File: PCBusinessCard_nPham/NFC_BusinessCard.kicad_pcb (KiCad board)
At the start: 2 copper layers, 85.6 x 68.1 mm, 20 parts

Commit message: front side done
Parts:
- removed the ? at (80.0, 43.1)
- removed the ? at (79.0, 46.2)
- removed the ? at (73.2, 47.8)
- moved LED1 21.1 mm to (94.0, 55.9)
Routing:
- net N$4: track 55.8 -> 54.4 mm, vias 2 -> 1
- net N$6: track 70.7 -> 69.3 mm, vias 2 -> 1

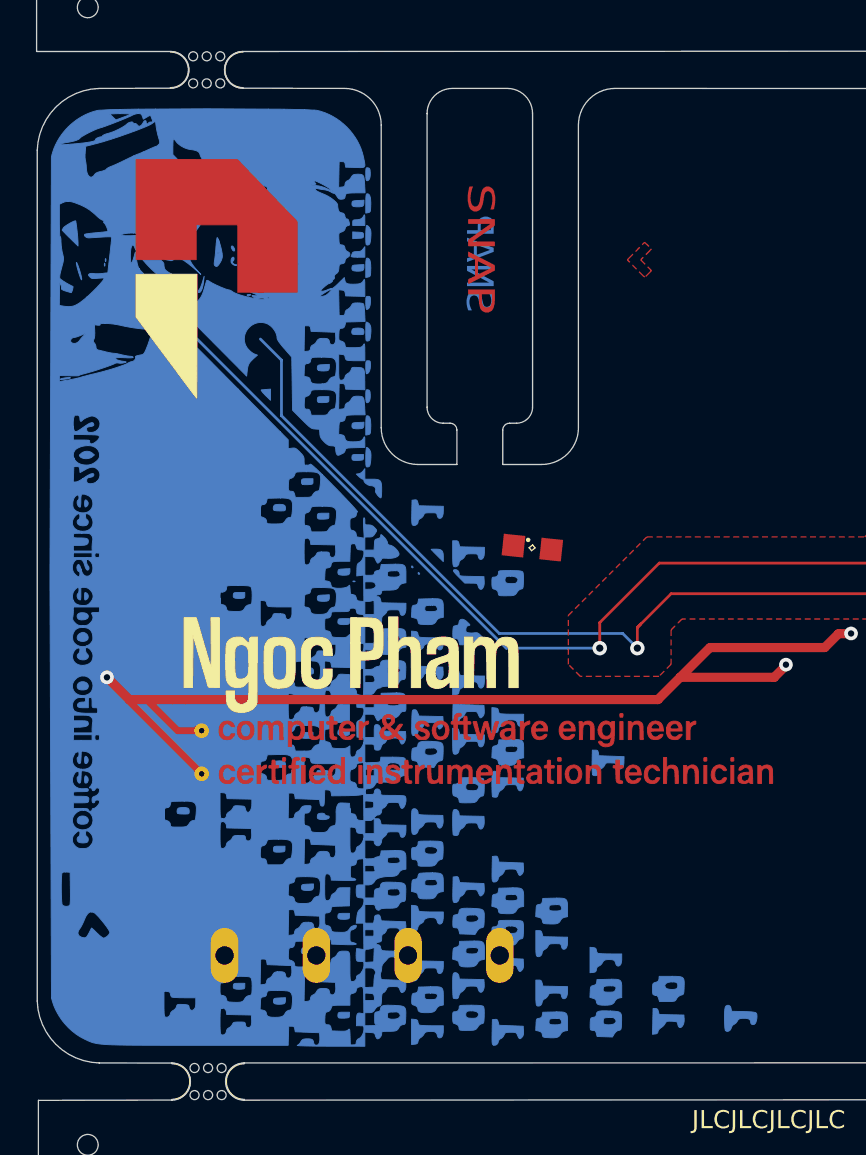
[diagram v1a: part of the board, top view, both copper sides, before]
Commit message: finished front and back side
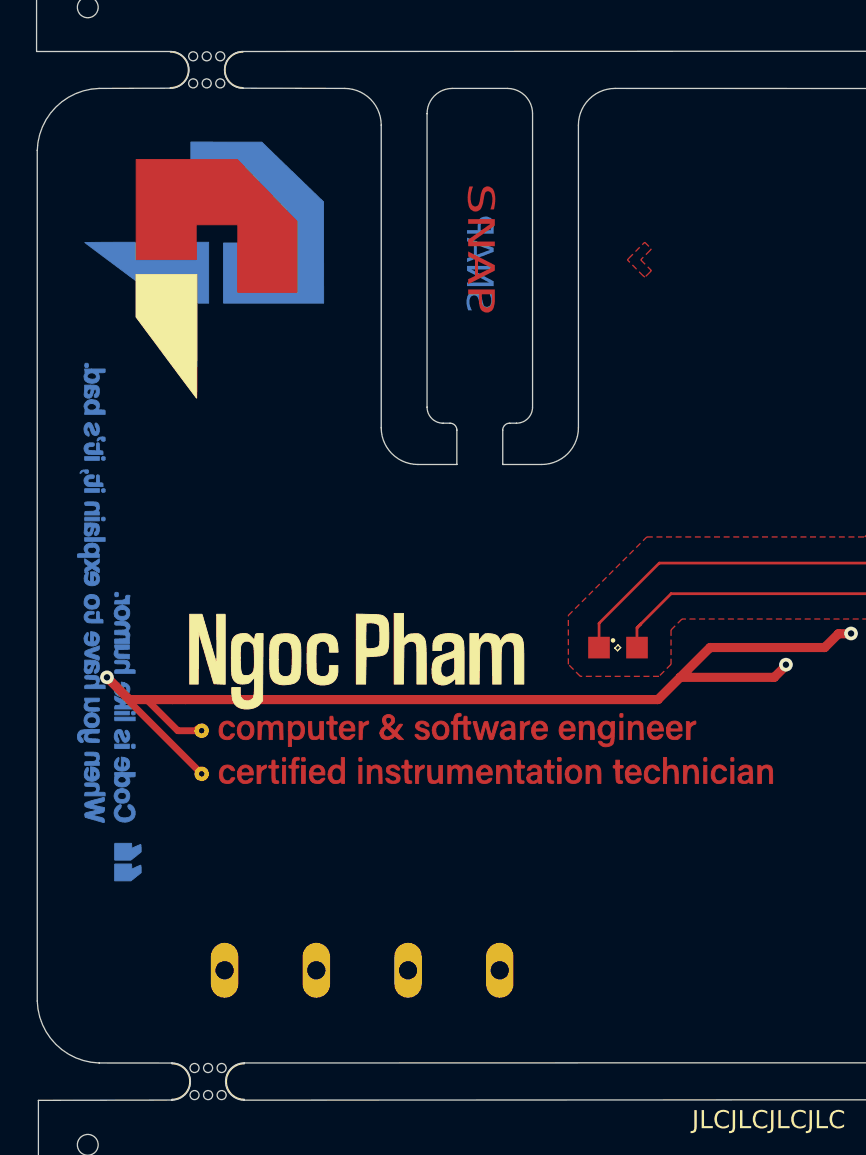
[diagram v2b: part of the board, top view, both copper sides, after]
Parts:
- moved LED1 7.29 mm to (98.7, 61.4), turned to 0 degrees
- moved CONTACT INFO 0.82 mm to (83.3, 79.3)
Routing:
- net N$6: track 69.3 -> 38.5 mm, vias 1 -> 0
- net N$4: track 54.4 -> 24.6 mm, vias 1 -> 0
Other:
- board text removed: "Glenn Lopez"

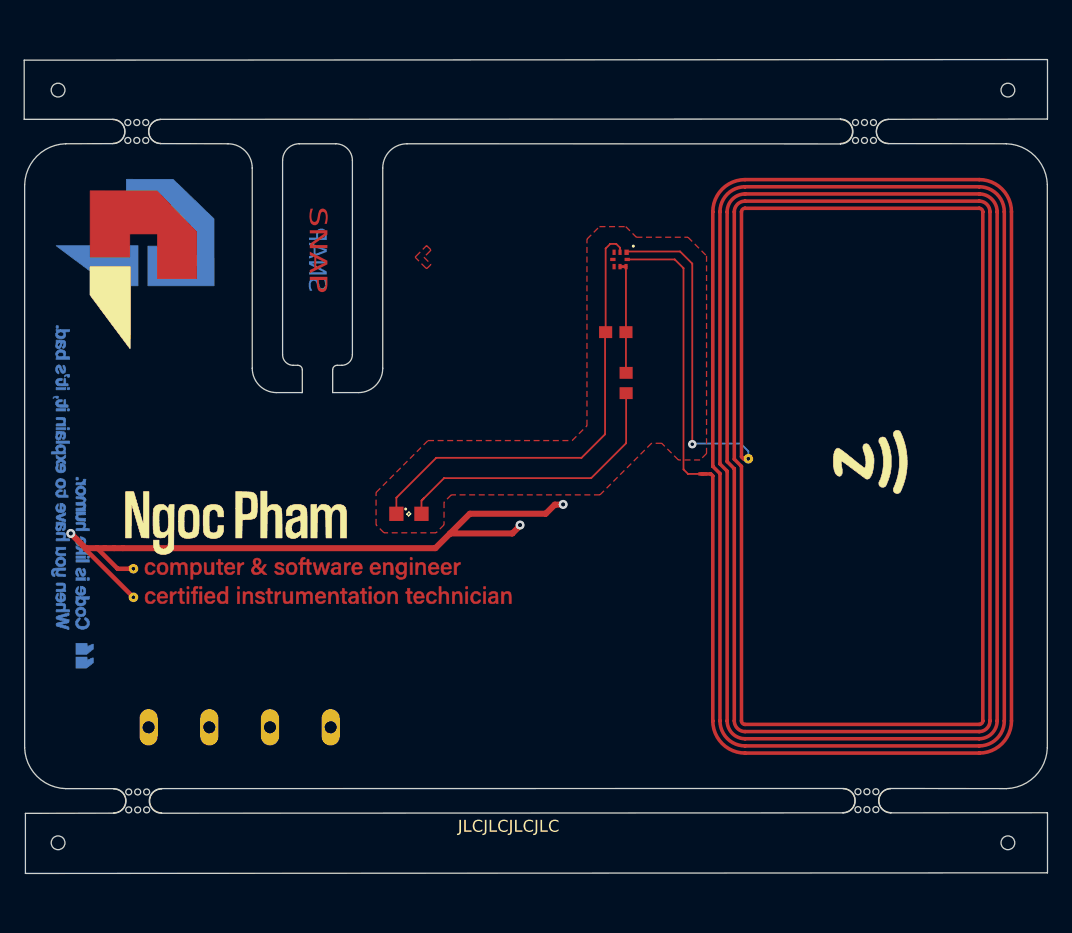
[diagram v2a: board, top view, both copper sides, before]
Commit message: added fiducial support to rails
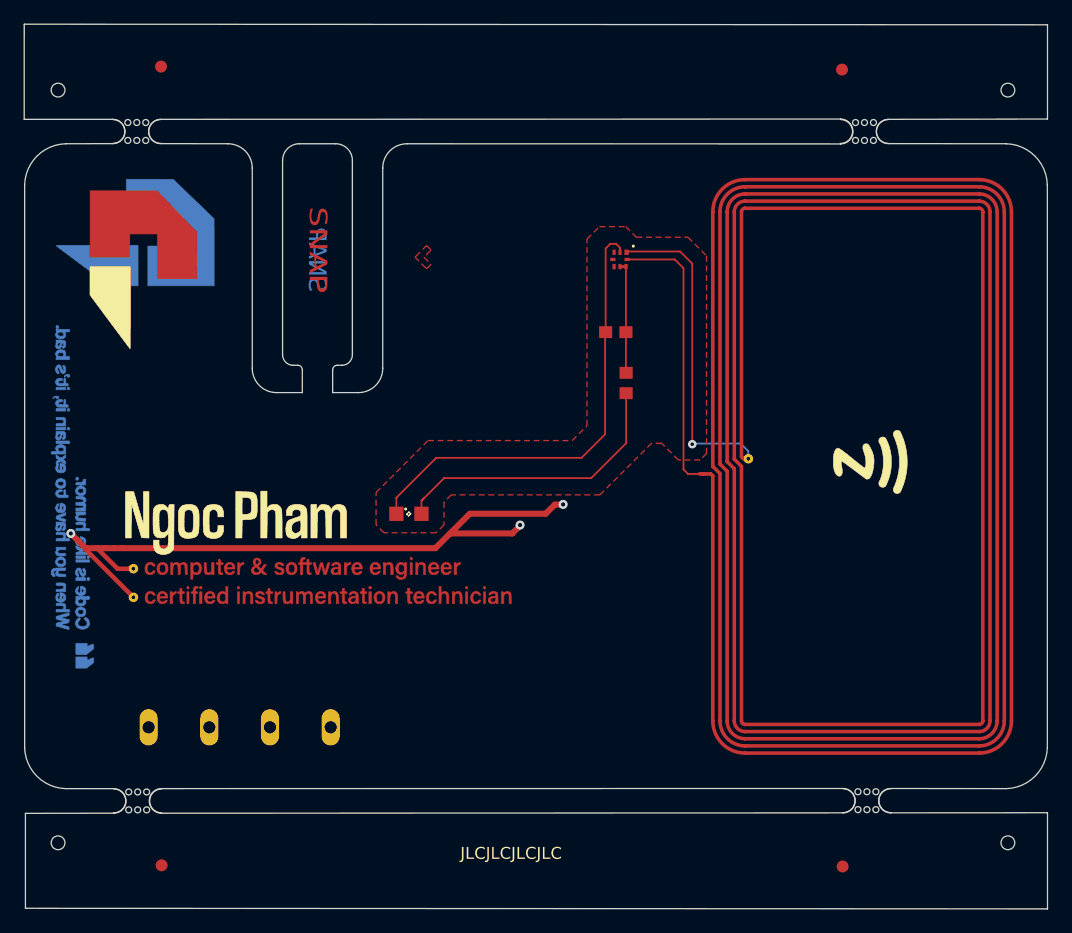
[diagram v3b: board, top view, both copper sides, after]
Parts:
- added REF**: Fiducial, Fiducial:Fiducial_1mm_Mask2mm, F.Cu at (135.0, 91.0)
- added REF**: Fiducial, Fiducial:Fiducial_1mm_Mask2mm, F.Cu at (78.0, 24.0)
- added REF**: Fiducial, Fiducial:Fiducial_1mm_Mask2mm, F.Cu at (78.0, 90.8)
- added REF**: Fiducial, Fiducial:Fiducial_1mm_Mask2mm, F.Cu at (134.9, 24.2)
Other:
- board size 85.6 x 68.1 mm -> 85.7 x 74 mm
